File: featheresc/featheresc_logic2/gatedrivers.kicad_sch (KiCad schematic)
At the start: 9 parts, among them U6 NCP81155MN, U7 NCP81155MN

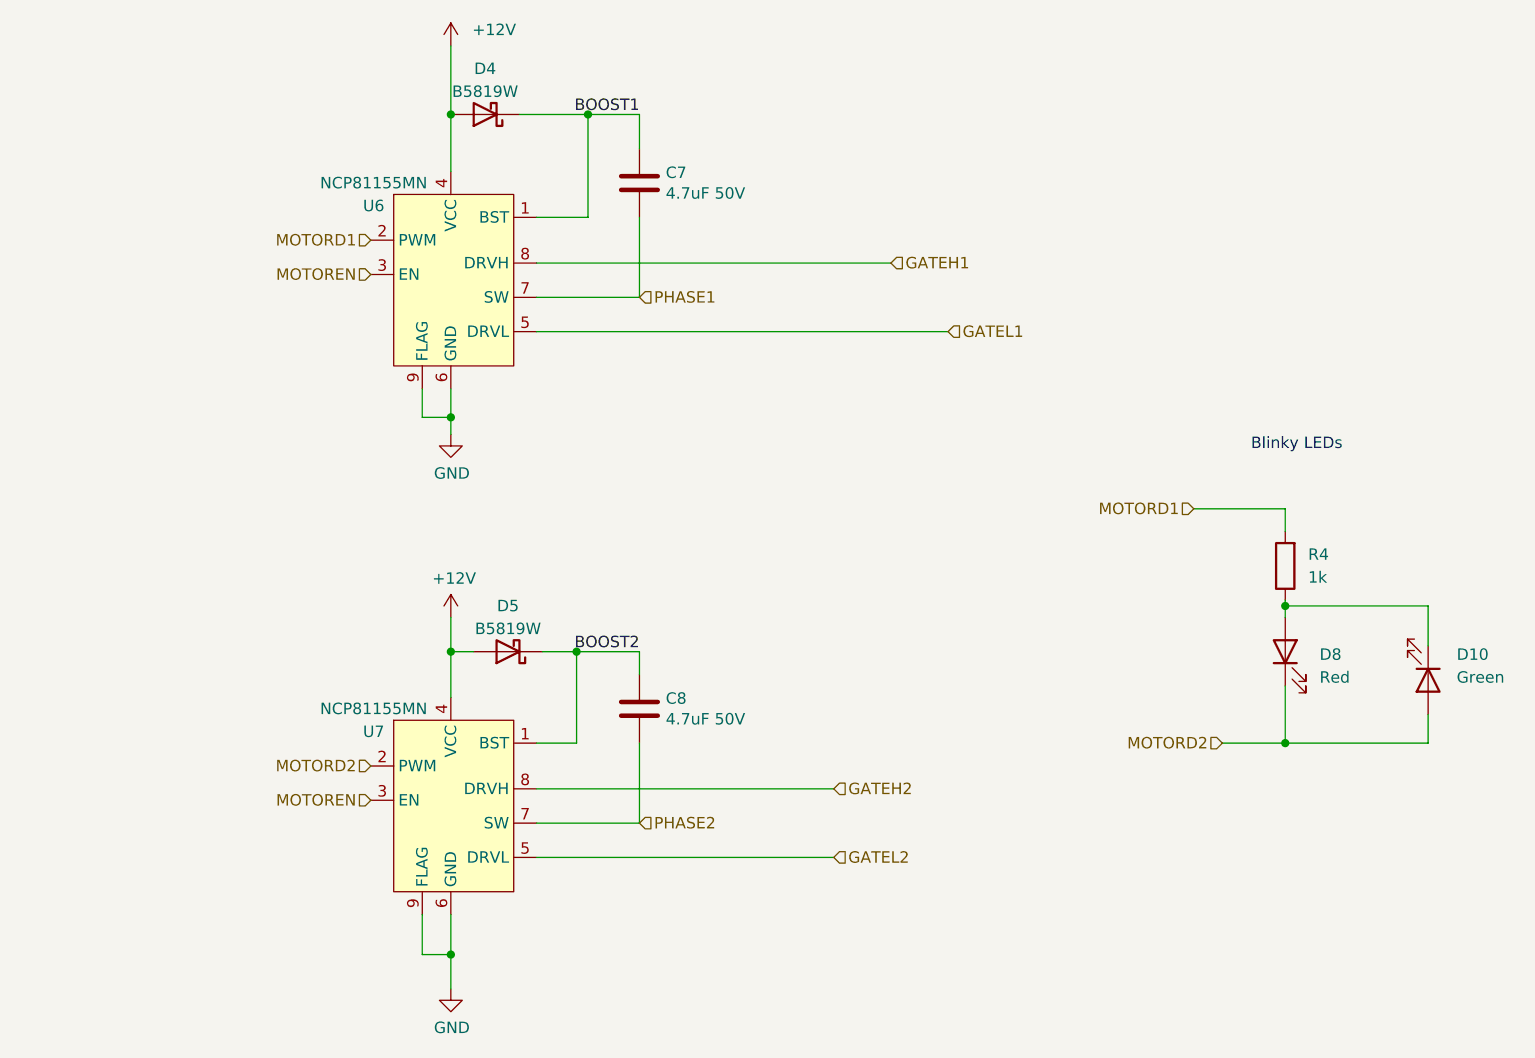
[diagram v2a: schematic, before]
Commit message: Pulldown EN pins
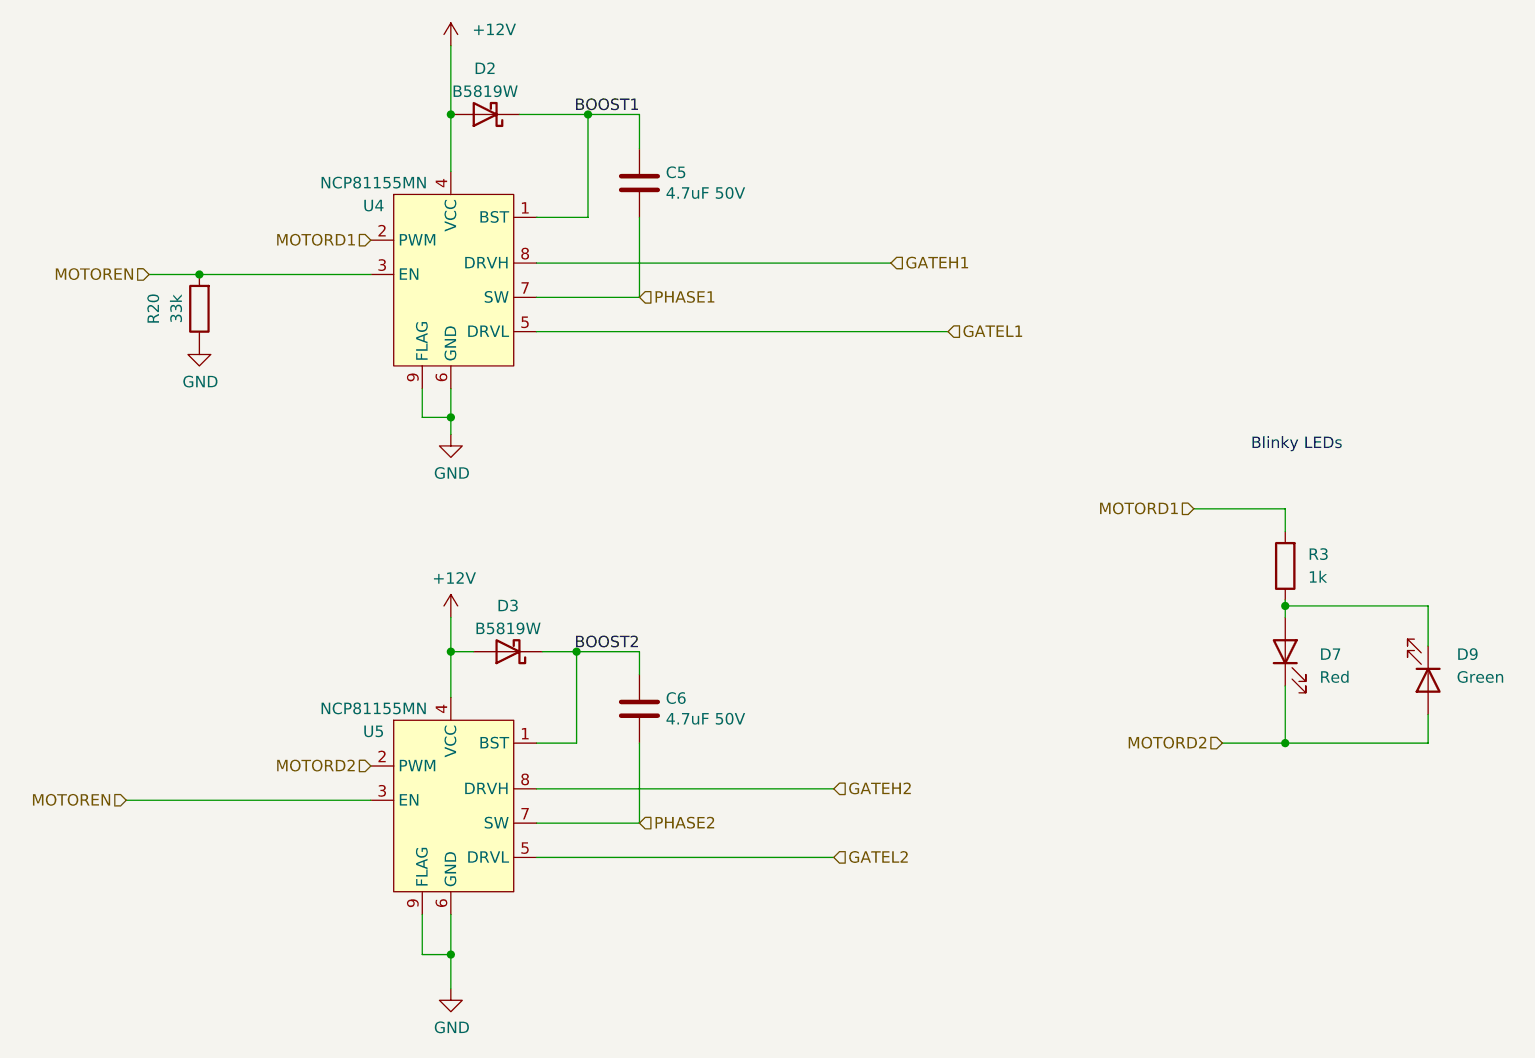
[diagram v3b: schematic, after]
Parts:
- added R20: 33k, Resistor_SMD:R_0603_1608Metric_Pad0.98x0.95mm_HandSolder, symbol Device:R
- renumbered C7 to C5, C8 to C6, D4 to D2, D5 to D3, D8 to D7, D10 to D9, R4 to R3, U6 to U4, U7 to U5
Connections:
- net GND: now also R20.1
- net MOTOREN: now also R20.2
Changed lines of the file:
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@@
   (junction (at 68.58 146.685) (diameter 0.9144) (color 0 0 0 0)
   )
+  (junction (at 40.64 71.12) (diameter 0) (color 0 0 0 0)
+  )
   (junction (at 68.58 113.03) (diameter 0.9144) (color 0 0 0 0)
   )
@@
     (stroke (width 0) (type solid) (color 0 0 0 0))
   )
+  (wire (pts (xy 40.64 71.12) (xy 59.69 71.12))
+    (stroke (width 0) (type default) (color 0 0 0 0))
+  )
   (wire (pts (xy 76.2 53.34) (xy 83.82 53.34))
     (stroke (width 0) (type solid) (color 0 0 0 0))
@@
     (stroke (width 0) (type solid) (color 0 0 0 0))
   )
+  (wire (pts (xy 32.512 129.54) (xy 59.69 129.54))
+    (stroke (width 0) (type default) (color 0 0 0 0))
+  )
   (wire (pts (xy 65.405 83.82) (xy 65.405 86.995))
     (stroke (width 0) (type solid) (color 0 0 0 0))
@@
   (wire (pts (xy 68.58 88.9) (xy 68.58 86.995))
     (stroke (width 0) (type solid) (color 0 0 0 0))
+  )
+  (wire (pts (xy 35.052 71.12) (xy 40.64 71.12))
+    (stroke (width 0) (type default) (color 0 0 0 0))
   )
   (wire (pts (xy 68.58 45.72) (xy 68.58 53.34))
@@
     (effects (font (size 1.27 1.27)) (justify right))
   )
-  (hierarchical_label "MOTOREN" (shape input) (at 59.69 71.12 180)
+  (hierarchical_label "MOTOREN" (shape input) (at 35.052 71.12 180)
     (effects (font (size 1.27 1.27)) (justify right))
   )
@@
     (effects (font (size 1.27 1.27)) (justify right))
   )
-  (hierarchical_label "MOTOREN" (shape input) (at 59.69 129.54 180)
+  (hierarchical_label "MOTOREN" (shape input) (at 32.512 129.54 180)
     (effects (font (size 1.27 1.27)) (justify right))
   )
@@
   (symbol (lib_id "Device:LED") (at 177.165 116.205 270)
     (in_bom yes) (on_board yes) (fields_autoplaced)
-    (property "Reference" "D10" (id 0) (at 180.34 113.3474 90)
+    (property "Reference" "D9" (id 0) (at 180.34 113.3474 90)
       (effects (font (size 1.27 1.27)) (justify left))
     )
@@
   (symbol (lib_id "Device:R") (at 161.29 103.505 180)
     (in_bom yes) (on_board yes) (fields_autoplaced)
-    (property "Reference" "R4" (id 0) (at 163.83 102.2349 0)
+    (property "Reference" "R3" (id 0) (at 163.83 102.2349 0)
       (effects (font (size 1.27 1.27)) (justify right))
     )
@@
   (symbol (lib_id "Device:C") (at 89.535 119.38 0)
     (in_bom yes) (on_board yes)
-    (property "Reference" "C8" (id 0) (at 92.456 118.231 0)
+    (property "Reference" "C6" (id 0) (at 92.456 118.231 0)
       (effects (font (size 1.27 1.27)) (justify left))
     )
@@
     (pin "2")
   )
+  (symbol (lib_id "Device:R") (at 40.64 74.93 180)
+    (in_bom yes) (on_board yes)
+    (property "Reference" "R20" (id 0) (at 35.56 74.93 90))
+    (property "Value" "33k" (id 1) (at 38.1 74.93 90))
+    (property "Footprint" "Resistor_SMD:R_0603_1608Metric_Pad0.98x0.95mm_HandSolder" (id 2) (at 42.418 74.93 90)
+      (effects (font (size 1.27 1.27)) hide)
+    )
+    (property "Datasheet" "~" (id 3) (at 40.64 74.93 0)
+      (effects (font (size 1.27 1.27)) hide)
+    )
+    (pin "1")
+    (pin "2")
+  )
   (symbol (lib_id "featheresc_logic:NCP81155MN") (at 68.58 132.08 0)
     (in_bom yes) (on_board yes)
-    (property "Reference" "U7" (id 0) (at 60.0075 121.92 0))
+    (property "Reference" "U5" (id 0) (at 60.0075 121.92 0))
     (property "Value" "NCP81155MN" (id 1) (at 60.0075 119.38 0))
     (property "Footprint" "Package_DFN_QFN:DFN-8-1EP_3x3mm_P0.5mm_EP1.66x2.38mm" (id 2) (at 68.58 132.08 0)
@@
   (symbol (lib_id "Device:LED") (at 161.29 113.03 90)
     (in_bom yes) (on_board yes) (fields_autoplaced)
-    (property "Reference" "D8" (id 0) (at 165.1 113.3474 90)
+    (property "Reference" "D7" (id 0) (at 165.1 113.3474 90)
       (effects (font (size 1.27 1.27)) (justify right))
     )
@@
   (symbol (lib_id "power:GND") (at 68.58 88.9 0)
     (in_bom yes) (on_board yes)
-    (property "Reference" "#PWR013" (id 0) (at 68.58 95.25 0)
+    (property "Reference" "#PWR09" (id 0) (at 68.58 95.25 0)
       (effects (font (size 1.27 1.27)) hide)
     )
@@
   (symbol (lib_id "Device:C") (at 89.535 60.96 0)
     (in_bom yes) (on_board yes)
-    (property "Reference" "C7" (id 0) (at 92.4561 59.8106 0)
+    (property "Reference" "C5" (id 0) (at 92.4561 59.8106 0)
       (effects (font (size 1.27 1.27)) (justify left))
     )
@@
   (symbol (lib_id "power:GND") (at 68.58 150.495 0)
     (in_bom yes) (on_board yes)
-    (property "Reference" "#PWR015" (id 0) (at 68.58 156.845 0)
+    (property "Reference" "#PWR011" (id 0) (at 68.58 156.845 0)
       (effects (font (size 1.27 1.27)) hide)
     )
@@
   (symbol (lib_id "power:+12V") (at 68.58 109.22 0)
     (in_bom yes) (on_board yes)
-    (property "Reference" "#PWR014" (id 0) (at 68.58 113.03 0)
+    (property "Reference" "#PWR010" (id 0) (at 68.58 113.03 0)
       (effects (font (size 1.27 1.27)) hide)
     )
@@
   (symbol (lib_id "Device:D_Schottky") (at 72.39 53.34 180)
     (in_bom yes) (on_board yes) (fields_autoplaced)
-    (property "Reference" "D4" (id 0) (at 72.39 48.26 0))
+    (property "Reference" "D2" (id 0) (at 72.39 48.26 0))
     (property "Value" "B5819W" (id 1) (at 72.39 50.8 0))
     (property "Footprint" "Diode_SMD:D_SOD-123" (id 2) (at 72.39 53.34 0)
@@
   (symbol (lib_id "featheresc_logic:NCP81155MN") (at 68.58 73.66 0)
     (in_bom yes) (on_board yes)
-    (property "Reference" "U6" (id 0) (at 60.0075 63.5 0))
+    (property "Reference" "U4" (id 0) (at 60.0075 63.5 0))
     (property "Value" "NCP81155MN" (id 1) (at 60.0075 60.96 0))
     (property "Footprint" "Package_DFN_QFN:DFN-8-1EP_3x3mm_P0.5mm_EP1.66x2.38mm" (id 2) (at 68.58 73.66 0)
@@
   (symbol (lib_id "power:+12V") (at 68.58 45.72 0)
     (in_bom yes) (on_board yes)
-    (property "Reference" "#PWR012" (id 0) (at 68.58 49.53 0)
+    (property "Reference" "#PWR08" (id 0) (at 68.58 49.53 0)
       (effects (font (size 1.27 1.27)) hide)
     )
@@
   (symbol (lib_id "Device:D_Schottky") (at 74.93 113.03 180)
     (in_bom yes) (on_board yes) (fields_autoplaced)
-    (property "Reference" "D5" (id 0) (at 74.93 107.95 0))
+    (property "Reference" "D3" (id 0) (at 74.93 107.95 0))
     (property "Value" "B5819W" (id 1) (at 74.93 110.49 0))
     (property "Footprint" "Diode_SMD:D_SOD-123" (id 2) (at 74.93 113.03 0)
@@
     (pin "2")
   )
+  (symbol (lib_id "power:GND") (at 40.64 78.74 0)
+    (in_bom yes) (on_board yes)
+    (property "Reference" "#PWR019" (id 0) (at 40.64 85.09 0)
+      (effects (font (size 1.27 1.27)) hide)
+    )
+    (property "Value" "GND" (id 1) (at 40.7543 83.0644 0))
+    (property "Footprint" "" (id 2) (at 40.64 78.74 0)
+      (effects (font (size 1.27 1.27)) hide)
+    )
+    (property "Datasheet" "" (id 3) (at 40.64 78.74 0)
+      (effects (font (size 1.27 1.27)) hide)
+    )
+    (pin "1")
+  )
 )

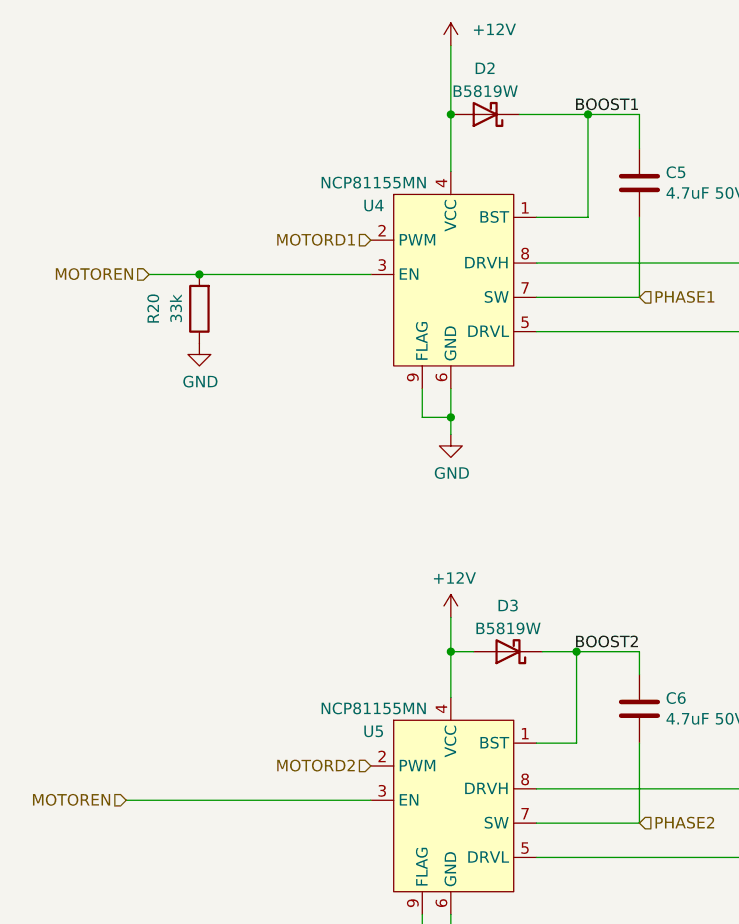
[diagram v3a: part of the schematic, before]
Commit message: Featheresc logic: add more decoupling caps etc
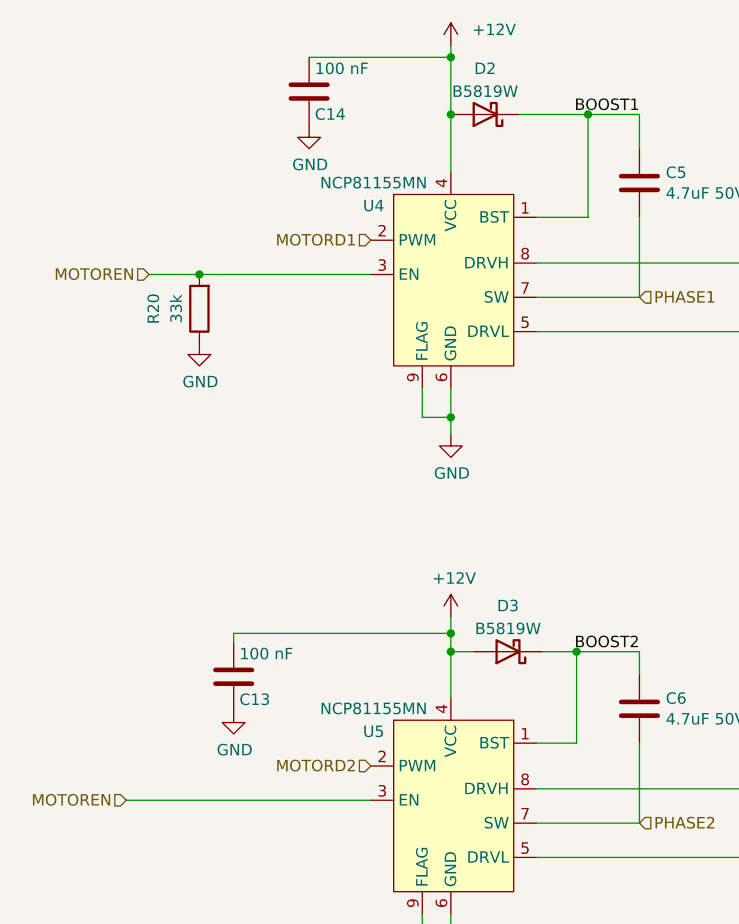
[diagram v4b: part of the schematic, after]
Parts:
- added C13, C14: 100 nF, Capacitor_SMD:C_0603_1608Metric_Pad1.08x0.95mm_HandSolder, symbol Device:C
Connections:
- net +12V: now also C13.1, C14.1
- net GND: now also C13.2, C14.2
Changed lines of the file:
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@@
   (junction (at 161.29 107.95) (diameter 0) (color 0 0 0 0)
   )
+  (junction (at 68.58 46.99) (diameter 0) (color 0 0 0 0)
+  )
   (junction (at 68.58 146.685) (diameter 0.9144) (color 0 0 0 0)
   )
@@
   (junction (at 68.58 113.03) (diameter 0.9144) (color 0 0 0 0)
   )
+  (junction (at 68.58 110.998) (diameter 0) (color 0 0 0 0)
+  )
   (junction (at 82.55 113.03) (diameter 0.9144) (color 0 0 0 0)
   )
@@
     (stroke (width 0) (type solid) (color 0 0 0 0))
   )
+  (wire (pts (xy 44.45 110.998) (xy 68.58 110.998))
+    (stroke (width 0) (type default) (color 0 0 0 0))
+  )
   (wire (pts (xy 177.165 107.95) (xy 177.165 112.395))
     (stroke (width 0) (type default) (color 0 0 0 0))
@@
     (stroke (width 0) (type default) (color 0 0 0 0))
   )
+  (wire (pts (xy 52.832 46.99) (xy 68.58 46.99))
+    (stroke (width 0) (type default) (color 0 0 0 0))
+  )
   (wire (pts (xy 161.29 123.19) (xy 154.305 123.19))
     (stroke (width 0) (type default) (color 0 0 0 0))
   )
-  (wire (pts (xy 68.58 109.22) (xy 68.58 113.03))
+  (wire (pts (xy 68.58 109.22) (xy 68.58 110.998))
     (stroke (width 0) (type solid) (color 0 0 0 0))
   )
@@
     (stroke (width 0) (type solid) (color 0 0 0 0))
   )
+  (wire (pts (xy 68.58 110.998) (xy 68.58 113.03))
+    (stroke (width 0) (type solid) (color 0 0 0 0))
+  )
   (wire (pts (xy 68.58 113.03) (xy 71.12 113.03))
     (stroke (width 0) (type solid) (color 0 0 0 0))
@@
     (stroke (width 0) (type default) (color 0 0 0 0))
   )
-  (wire (pts (xy 68.58 45.72) (xy 68.58 53.34))
+  (wire (pts (xy 44.45 112.014) (xy 44.45 110.998))
+    (stroke (width 0) (type default) (color 0 0 0 0))
+  )
+  (wire (pts (xy 68.58 45.72) (xy 68.58 46.99))
+    (stroke (width 0) (type solid) (color 0 0 0 0))
+  )
+  (wire (pts (xy 68.58 46.99) (xy 68.58 53.34))
     (stroke (width 0) (type solid) (color 0 0 0 0))
   )
@@
     (pin "2")
   )
+  (symbol (lib_id "power:GND") (at 44.45 119.634 0)
+    (in_bom yes) (on_board yes)
+    (property "Reference" "#PWR027" (id 0) (at 44.45 125.984 0)
+      (effects (font (size 1.27 1.27)) hide)
+    )
+    (property "Value" "GND" (id 1) (at 44.5643 123.9584 0))
+    (property "Footprint" "" (id 2) (at 44.45 119.634 0)
+      (effects (font (size 1.27 1.27)) hide)
+    )
+    (property "Datasheet" "" (id 3) (at 44.45 119.634 0)
+      (effects (font (size 1.27 1.27)) hide)
+    )
+    (pin "1")
+  )
   (symbol (lib_id "power:GND") (at 68.58 88.9 0)
     (in_bom yes) (on_board yes)
@@
     (pin "2")
   )
+  (symbol (lib_id "Device:C") (at 52.832 50.8 0)
+    (in_bom yes) (on_board yes)
+    (property "Reference" "C14" (id 0) (at 53.467 53.34 0)
+      (effects (font (size 1.27 1.27)) (justify left))
+    )
+    (property "Value" "100 nF" (id 1) (at 53.467 48.26 0)
+      (effects (font (size 1.27 1.27)) (justify left))
+    )
+    (property "Footprint" "Capacitor_SMD:C_0603_1608Metric_Pad1.08x0.95mm_HandSolder" (id 2) (at 53.7972 54.61 0)
+      (effects (font (size 1.27 1.27)) hide)
+    )
+    (property "Datasheet" "~" (id 3) (at 52.832 50.8 0)
+      (effects (font (size 1.27 1.27)) hide)
+    )
+    (pin "1")
+    (pin "2")
+  )
   (symbol (lib_id "power:GND") (at 68.58 150.495 0)
     (in_bom yes) (on_board yes)
@@
       (effects (font (size 1.27 1.27)) hide)
     )
+    (pin "1")
+  )
+  (symbol (lib_id "Device:C") (at 44.45 115.824 0)
+    (in_bom yes) (on_board yes)
+    (property "Reference" "C13" (id 0) (at 45.085 118.364 0)
+      (effects (font (size 1.27 1.27)) (justify left))
+    )
+    (property "Value" "100 nF" (id 1) (at 45.085 113.284 0)
+      (effects (font (size 1.27 1.27)) (justify left))
+    )
+    (property "Footprint" "Capacitor_SMD:C_0603_1608Metric_Pad1.08x0.95mm_HandSolder" (id 2) (at 45.4152 119.634 0)
+      (effects (font (size 1.27 1.27)) hide)
+    )
+    (property "Datasheet" "~" (id 3) (at 44.45 115.824 0)
+      (effects (font (size 1.27 1.27)) hide)
+    )
+    (pin "1")
+    (pin "2")
+  )
+  (symbol (lib_id "power:GND") (at 52.832 54.61 0)
+    (in_bom yes) (on_board yes)
+    (property "Reference" "#PWR029" (id 0) (at 52.832 60.96 0)
+      (effects (font (size 1.27 1.27)) hide)
+    )
+    (property "Value" "GND" (id 1) (at 52.9463 58.9344 0))
+    (property "Footprint" "" (id 2) (at 52.832 54.61 0)
+      (effects (font (size 1.27 1.27)) hide)
+    )
+    (property "Datasheet" "" (id 3) (at 52.832 54.61 0)
+      (effects (font (size 1.27 1.27)) hide)
+    )
